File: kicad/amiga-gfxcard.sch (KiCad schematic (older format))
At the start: 33 parts, among them P1 CONN_01X04, P2 CONN_01X16, P3 CONN_01X16, P4 CONN_01X16, P5 CONN_01X04, P6 CONN_01X04, P7 CONN_01X08, U1 TXB0108, U10 SN74CBT16233, U12 VGA, U2 TXB0108, U3 TXB0108, U4 TXB0108, U5 TXB0108, U6 TXB0108, U7 ADV7125-lqfp48, U8 SN74CBT16233, U9 74LS04

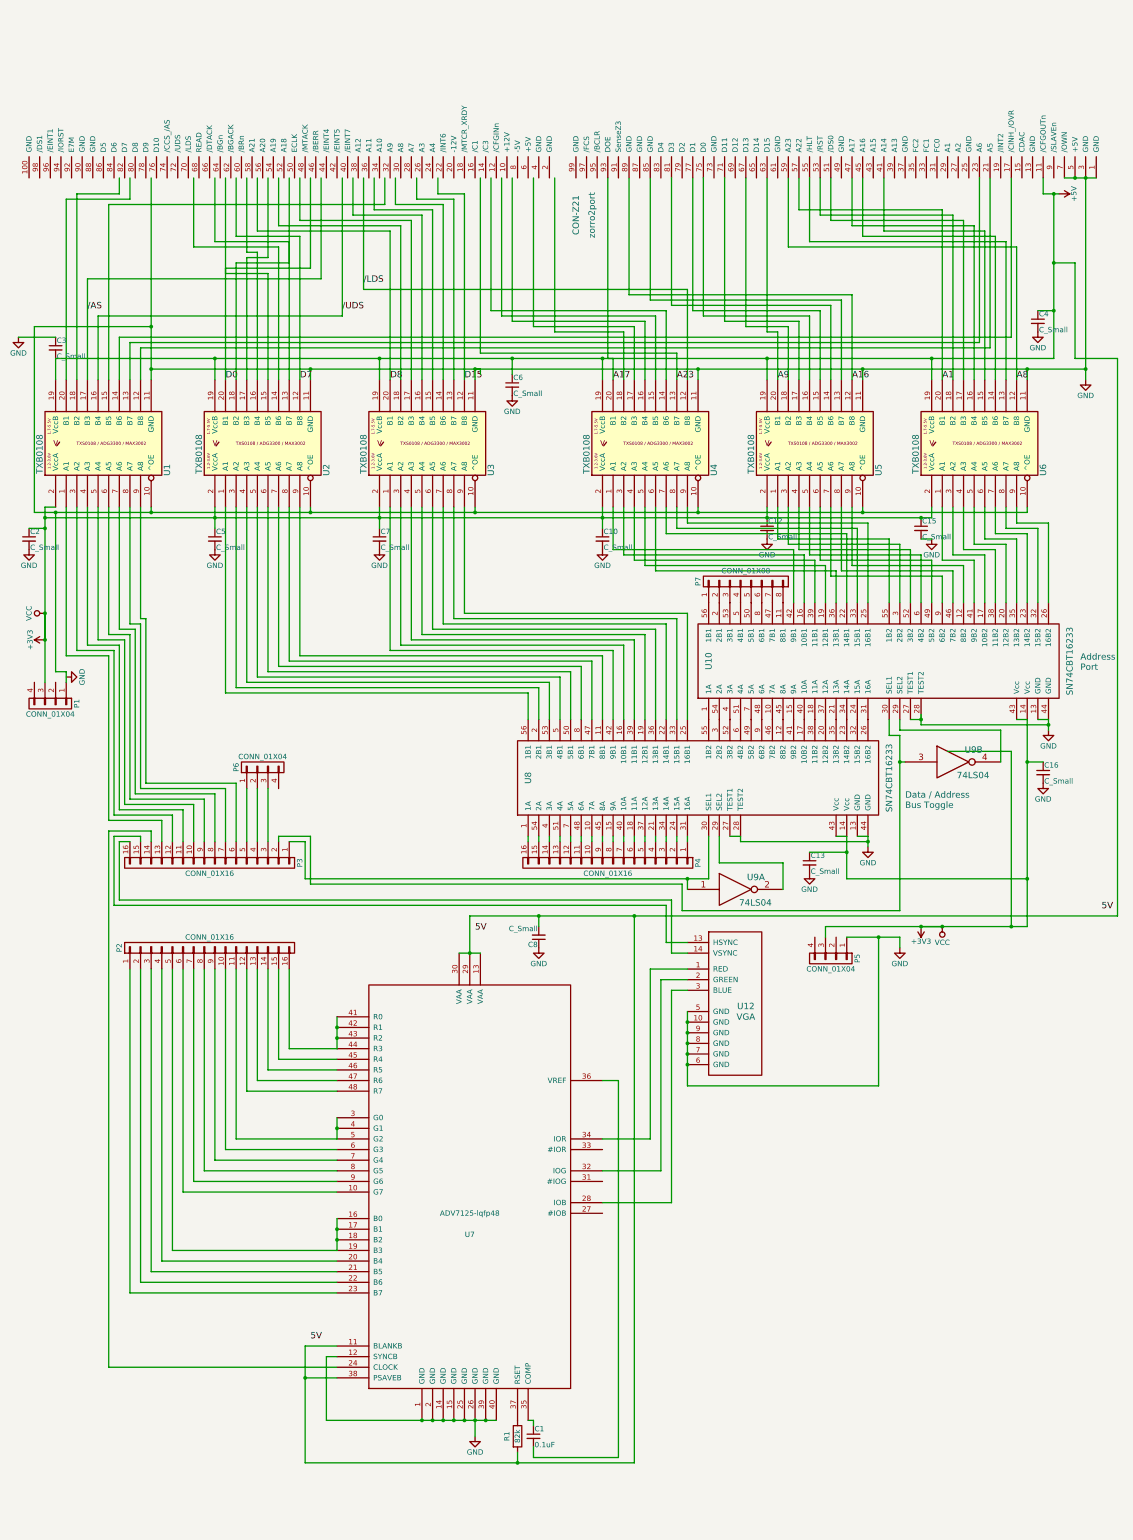
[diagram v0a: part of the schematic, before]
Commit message: WIP of simpler redesign for miniSpartan 6+
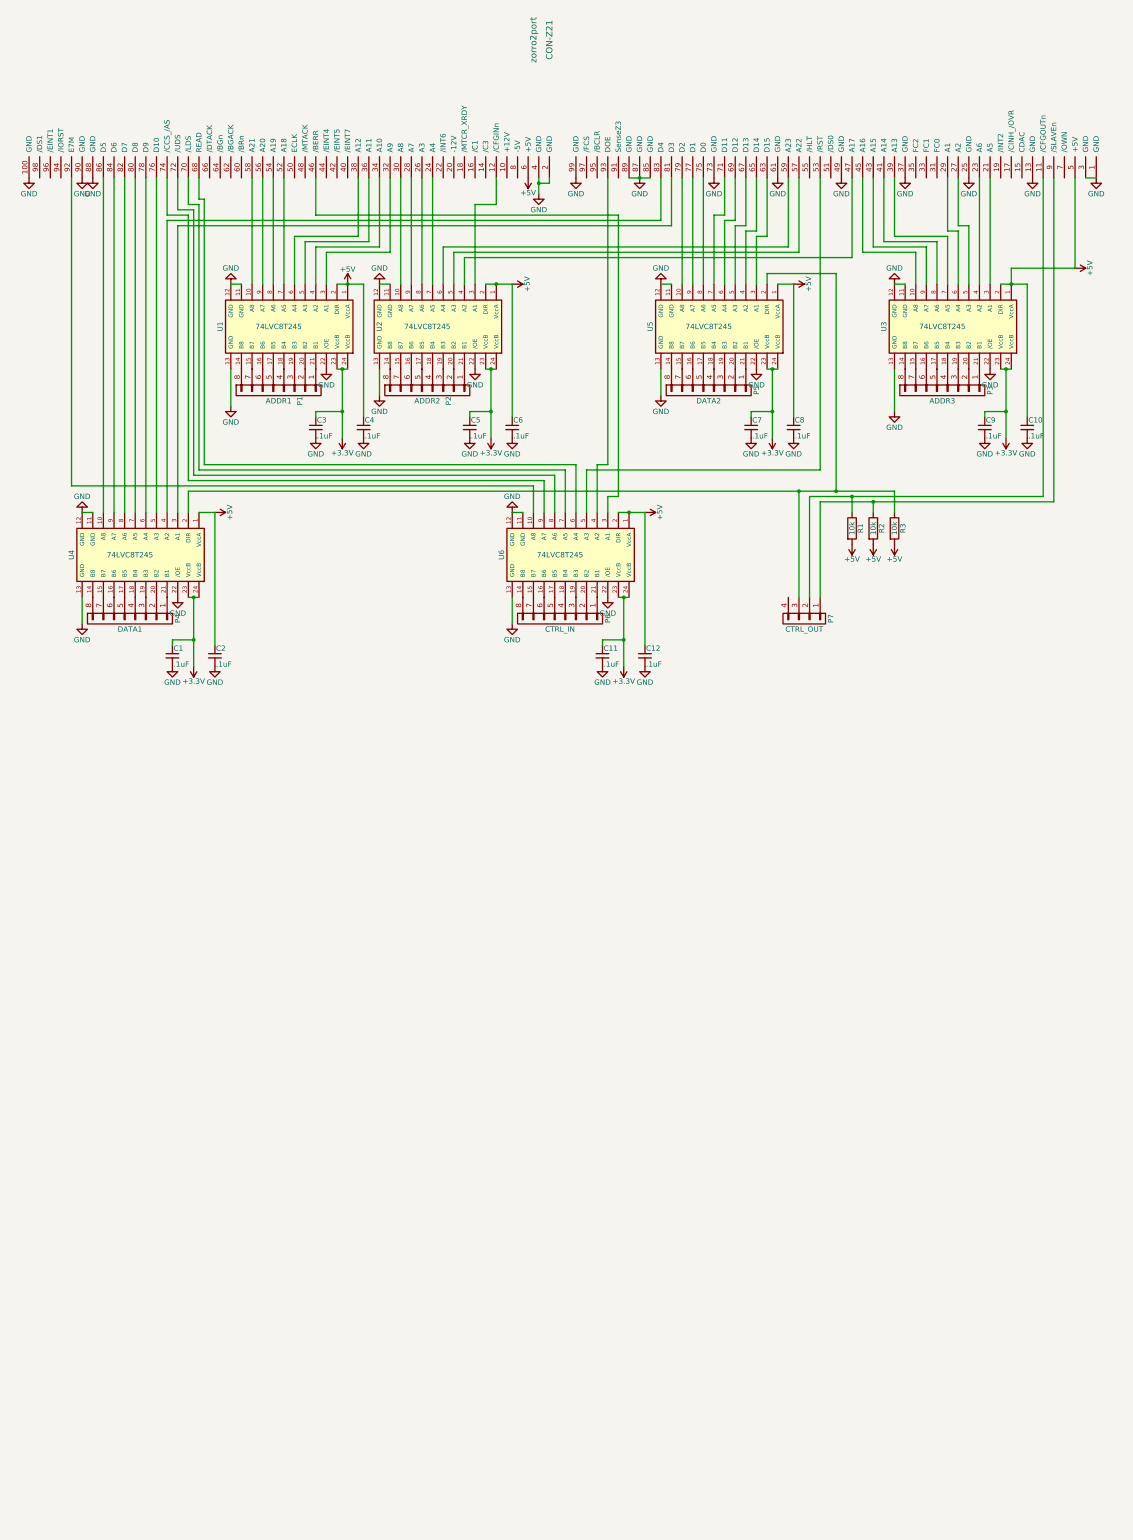
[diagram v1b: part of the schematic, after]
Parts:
- removed C13, C15, C16: C_Small, Capacitors_SMD:C_0603_HandSoldering, symbol C_Small
- removed P1, P5, P6: CONN_01X04, Pin_Headers:Pin_Header_Straight_1x04, symbol CONN_01X04
- removed P2, P3, P4: CONN_01X16, Pin_Headers:Pin_Header_Straight_1x16, symbol CONN_01X16
- removed U1, U2, U3, U4, U5, U6: TXB0108, opendous:TSSOP20_PW, symbol TXB0108
- removed U10, U8: SN74CBT16233, Housings_SSOP:SSOP-56_7.5x18.5mm_Pitch0.635mm, symbol SN74CBT16233
- removed U12: VGA, zorro2:HD15_B-HD15F, symbol VGA
- removed U7: ADV7125-lqfp48, Housings_QFP:LQFP-48_7x7mm_Pitch0.5mm, symbol ADV7125-lqfp48
- removed U9: 74LS04, Housings_SSOP:SSOP-14_5.3x6.2mm_Pitch0.65mm, symbol 74LS04
- added C11, C9: .1uF, Capacitors_ThroughHole:C_Rect_L4_W2.5_P2.5, symbol C_Small
- added P1: ADDR1, Pin_Headers:Pin_Header_Straight_1x08, symbol CONN_01X08
- added P2: ADDR2, Pin_Headers:Pin_Header_Straight_1x08, symbol CONN_01X08
- added P3: ADDR3, Pin_Headers:Pin_Header_Straight_1x08, symbol CONN_01X08
- added P5: DATA2, Pin_Headers:Pin_Header_Straight_1x08, symbol CONN_01X08
- added P6: CTRL_IN, Pin_Headers:Pin_Header_Straight_1x08, symbol CONN_01X08
- added P7: CTRL_OUT, Pin_Headers:Pin_Header_Straight_1x04, symbol CONN_01X04
- added R2, R3: 10k, Resistors_ThroughHole:Resistor_Horizontal_RM7mm, symbol R
- added U1, U2, U3, U4, U5, U6: 74LVC8T245, mnt:TSSOP24-44, symbol 74LVC8T245
- C1: value 0.1uF -> .1uF; footprint Capacitors_ThroughHole:C_Disc_D3_P2.5 -> Capacitors_ThroughHole:C_Rect_L4_W2.5_P2.5
- C10, C12, C2, C3, C4, C5, C6, C7, C8: value C_Small -> .1uF; footprint Capacitors_SMD:C_0603_HandSoldering -> Capacitors_ThroughHole:C_Rect_L4_W2.5_P2.5
- P4: renamed from P7; value CONN_01X08 -> DATA1
- R1: value 82k -> 10k; footprint Resistors_ThroughHole:Resistor_Horizontal_RM10mm -> Resistors_ThroughHole:Resistor_Horizontal_RM7mm
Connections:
- net labels added: +3.3V
- net labels removed: +3V3, /AS, /LDS, /UDS, 5V, A1, A16, A17, A23, A8, A9, D0, D15, D7, D8, VCC
- wire segments 517 -> 187
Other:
- note removed: "Address\nPort"
- note removed: "Data / Address \nBus Toggle"
- moved on the sheet: C4, P4

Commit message: redo of mk2 board finished
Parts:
- added P10: AUX1B, Pin_Headers:Pin_Header_Straight_1x08, symbol CONN_01X08
- added P11: AUX2A, Pin_Headers:Pin_Header_Straight_1x04, symbol CONN_01X04
- added P12: AUX2B, Pin_Headers:Pin_Header_Straight_1x04, symbol CONN_01X04
- added P8: CONN_01X02, Pin_Headers:Pin_Header_Straight_1x02, symbol CONN_01X02
- added P9: AUX1A, Pin_Headers:Pin_Header_Straight_1x08, symbol CONN_01X08
- C1, C10, C11, C12, C2, C3, C4, C5, C6, C7, C8, C9: footprint Capacitors_ThroughHole:C_Rect_L4_W2.5_P2.5 -> Capacitors_SMD:C_0805_HandSoldering
- P3: value ADDR3 -> ADDR4
- P4: value DATA1 -> DATA2
- P5: value DATA2 -> ADDR3
- P6: value CTRL_IN -> DATA1
- R1, R2, R3: footprint Resistors_ThroughHole:Resistor_Horizontal_RM7mm -> Resistors_SMD:R_1206_HandSoldering
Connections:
- net +3V3: now also P8.2 (P2)
- net +5V: now also U5.2 (DIR); no longer U2.2 (DIR)
- net GND: now also P8.1 (P1)
- net at CON-Z21.11 (/CFGOUTn), R1.1: now also P7.1 (P1); no longer P7.2 (P2)
- net at CON-Z21.21 (A5): now also U1.10 (A8); no longer U3.3 (A1)
- net at CON-Z21.23 (A6): now also U1.9 (A7); no longer U3.4 (A2)
- net at CON-Z21.24 (A4): now also U5.10 (A8); no longer U2.7 (A5)
- net at CON-Z21.26 (A3): now also U5.9 (A7); no longer U2.8 (A6)
- net at CON-Z21.27 (A2): now also U1.8 (A6); no longer U3.5 (A3)
- net at CON-Z21.28 (A7): now also U5.8 (A6); no longer U2.9 (A7)
- net at CON-Z21.29 (A1): now also U1.7 (A5); no longer U3.6 (A4)
- net at CON-Z21.30 (A8): now also U5.7 (A5); no longer U2.10 (A8)
- net at CON-Z21.32 (A9): now also U5.6 (A4); no longer U1.3 (A1)
- net at CON-Z21.34 (A10): now also U5.5 (A3); no longer U1.4 (A2)
- net at CON-Z21.36 (A11): now also U5.4 (A2); no longer U1.5 (A3)
- net at CON-Z21.38 (A12): now also U5.3 (A1); no longer U1.6 (A4)
- net at CON-Z21.39 (A13): now also U1.6 (A4); no longer U3.7 (A5)
- net at CON-Z21.41 (A14): now also U1.5 (A3); no longer U3.8 (A6)
- net at CON-Z21.43 (A15): now also U1.4 (A2); no longer U3.9 (A7)
- net at CON-Z21.45 (A16): now also U1.3 (A1); no longer U3.10 (A8)
- net at CON-Z21.46 (/BERR): now also U2.4 (A2); no longer U6.3 (A1)
- net at CON-Z21.47 (A17): now also U2.10 (A8); no longer U2.4 (A2)
- net at CON-Z21.52 (A18): now also U3.10 (A8); no longer U1.7 (A5)
- net at CON-Z21.53 (/RST): now also U2.5 (A3); no longer U6.5 (A3)
- net at CON-Z21.54 (A19): now also U3.9 (A7); no longer U1.8 (A6)
- net at CON-Z21.56 (A20): now also U3.8 (A6); no longer U1.9 (A7)
- net at CON-Z21.57 (A22): now also U2.9 (A7); no longer U2.5 (A3)
- net at CON-Z21.58 (A21): now also U3.7 (A5); no longer U1.10 (A8)
- net at CON-Z21.59 (A23): now also U2.8 (A6); no longer U2.6 (A4)
- net at CON-Z21.63 (D15): now also U6.10 (A8); no longer U5.3 (A1)
- net at CON-Z21.65 (D14): now also U6.9 (A7); no longer U5.4 (A2)
- net at CON-Z21.67 (D13): now also U6.8 (A6); no longer U5.5 (A3)
- net at CON-Z21.68 (READ): now also U3.6 (A4); no longer U6.6 (A4)
- net at CON-Z21.69 (D12): now also U6.7 (A5); no longer U5.6 (A4)
- net at CON-Z21.70 (/LDS): now also U3.5 (A3); no longer U6.7 (A5)
- net at CON-Z21.71 (D11): now also U6.6 (A4); no longer U5.7 (A5)
- net at CON-Z21.72 (/UDS): now also U3.4 (A2); no longer U6.8 (A6)
- net at CON-Z21.74 (/CCS_/AS): now also U3.3 (A1); no longer U6.9 (A7)
- net at CON-Z21.75 (D0): now also U6.5 (A3); no longer U5.8 (A6)
- net at CON-Z21.76 (D10): now also U4.10 (A8); no longer U4.5 (A3)
- net at CON-Z21.77 (D1): now also U6.4 (A2); no longer U5.9 (A7)
- net at CON-Z21.78 (D9): now also U4.9 (A7); no longer U4.6 (A4)
- net at CON-Z21.79 (D2): now also U6.3 (A1); no longer U5.10 (A8)
- net at CON-Z21.80 (D8): now also U4.8 (A6); no longer U4.7 (A5)
- net at CON-Z21.81 (D3): now also U4.4 (A2); no longer U4.3 (A1)
- net at CON-Z21.82 (D7): now also U4.7 (A5); no longer U4.8 (A6)
- net at CON-Z21.83 (D4): now also CON-Z21.92 (E7M), U2.6 (A4), U4.3 (A1); no longer U4.4 (A2)
- net at CON-Z21.84 (D6): now also U4.6 (A4); no longer U4.9 (A7)
- net at CON-Z21.86 (D5): now also U4.5 (A3); no longer U4.10 (A8)
- net at CON-Z21.9 (/SLAVEn), R2.1: now also P7.2 (P2); no longer P7.1 (P1)
- net at CON-Z21.93 (DOE): now also U2.7 (A5); no longer U6.4 (A2)
- net at R3.1, U4.2 (DIR): now also P7.4 (P4), U2.2 (DIR); no longer P7.3 (P3), U5.2 (DIR)
- new net: P10.1 (P1), P9.1 (P1)
- new net: P10.2 (P2), P9.2 (P2)
- new net: P10.3 (P3), P9.3 (P3)
- new net: P10.4 (P4), P9.4 (P4)
- new net: P10.5 (P5), P9.5 (P5)
- new net: P10.6 (P6), P9.6 (P6)
- new net: P10.7 (P7), P9.7 (P7)
- new net: P10.8 (P8), P9.8 (P8)
- new net: P11.1 (P1), P12.1 (P1)
- new net: P11.2 (P2), P12.2 (P2)
- new net: P11.3 (P3), P12.3 (P3)
- new net: P11.4 (P4), P12.4 (P4)
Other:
- moved on the sheet: C1, C10, C11, C12, C2, C3, C4, C5, C6, C7, C8, C9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

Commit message: board v1.2 finished
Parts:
- removed P10: AUX1B, Pin_Headers:Pin_Header_Straight_1x08, symbol CONN_01X08
- removed P11: AUX2A, Pin_Headers:Pin_Header_Straight_1x04, symbol CONN_01X04
- removed P12: AUX2B, Pin_Headers:Pin_Header_Straight_1x04, symbol CONN_01X04
- removed P7: CTRL_OUT, Pin_Headers:Pin_Header_Straight_1x04, symbol CONN_01X04
- removed P9: AUX1A, Pin_Headers:Pin_Header_Straight_1x08, symbol CONN_01X08
- added P13: X1, Pin_Headers:Pin_Header_Straight_1x08, symbol CONN_01X08
- added P14: X2, Pin_Headers:Pin_Header_Straight_1x08, symbol CONN_01X08
- added P16: D1, Pin_Headers:Pin_Header_Straight_1x03, symbol CONN_01X03
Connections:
- net +5V: now also U2.2 (DIR); no longer U6.2 (DIR)
- net at CON-Z21.11 (/CFGOUTn), R1.1: now also P16.1 (P1)
- net at CON-Z21.83 (D4), U4.3 (A1): no longer CON-Z21.92 (E7M), U2.6 (A4)
- net at CON-Z21.9 (/SLAVEn), R2.1: now also P16.2 (P2)
- net at P4.1 (P1): no longer U4.21 (B1)
- net at P4.5 (P5): no longer U4.17 (B5)
- net at P1.1 (P1): no longer U1.21 (B1)
- net at P1.5 (P5): no longer U1.17 (B5)
- net at P2.1 (P1): no longer U2.21 (B1)
- net at P2.5 (P5): no longer U2.17 (B5)
- net at P6.1 (P1): no longer U6.21 (B1)
- net at P6.5 (P5): no longer U6.17 (B5)
- net at P5.1 (P1): no longer U5.21 (B1)
- net at P5.5 (P5): no longer U5.17 (B5)
- net at P3.1 (P1): no longer U3.21 (B1)
- net at P3.5 (P5): no longer U3.17 (B5)
- net at R3.1, U4.2 (DIR): now also U6.2 (DIR), P16.3 (P3); no longer U2.2 (DIR)
- new net: CON-Z21.92 (E7M), U2.6 (A4)
- new net: P13.8 (P8), U1.17 (B5)
- new net: P13.7 (P7), U1.21 (B1)
- new net: P14.8 (P8), U2.17 (B5)
- new net: P14.7 (P7), U2.21 (B1)
- new net: P14.6 (P6), U5.17 (B5)
- new net: P14.4 (P4), U5.21 (B1)
- new net: P14.3 (P3), U3.17 (B5)
- new net: P14.2 (P2), U3.21 (B1)
- new net: P13.6 (P6), U4.17 (B5)
- new net: P13.4 (P4), U4.21 (B1)
- new net: P13.3 (P3), U6.17 (B5)
- new net: P13.2 (P2), U6.21 (B1)
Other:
- moved on the sheet: C11, C12, C3, C4, C5, C6, P1, P2, P3, P4, P5, P6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

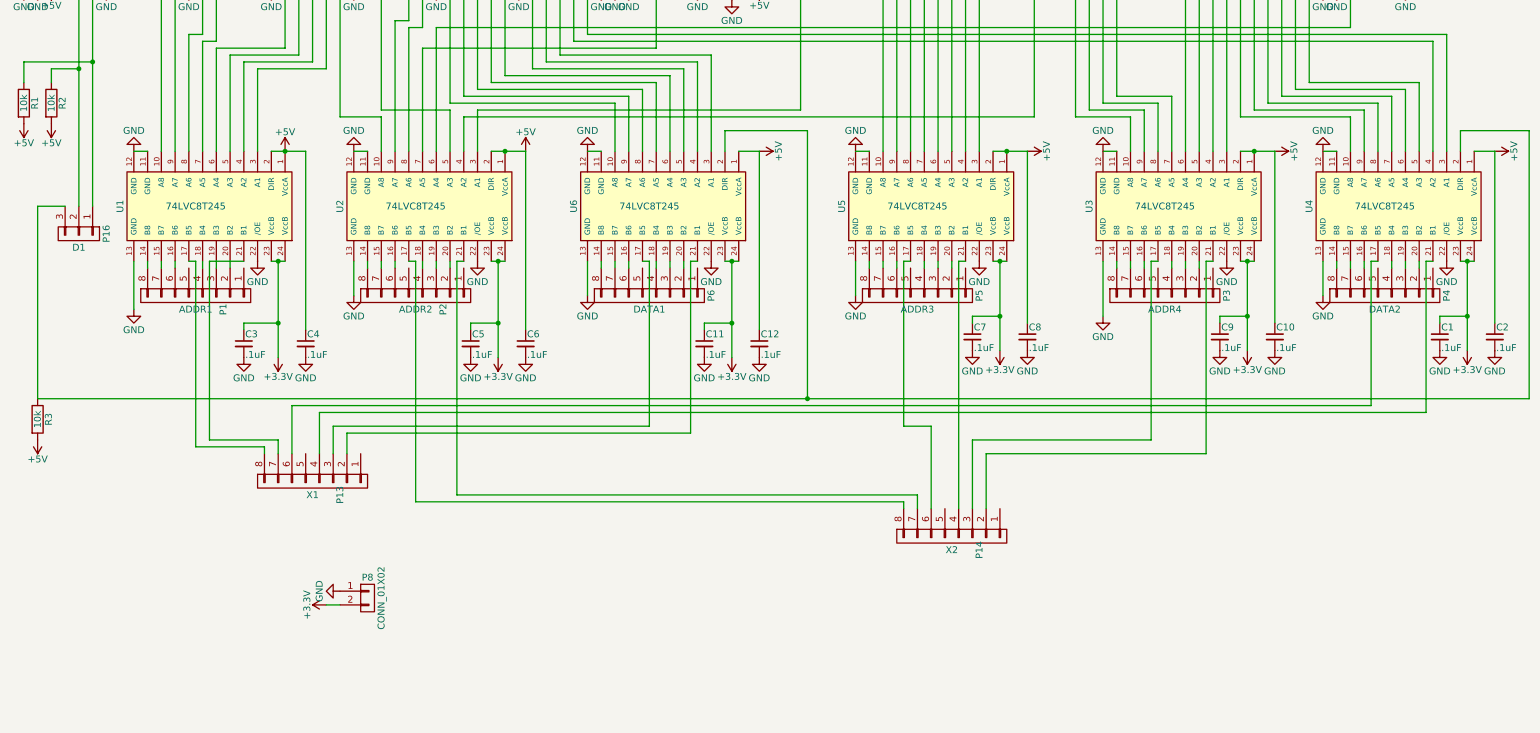
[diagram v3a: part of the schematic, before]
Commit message: Version 2, new board, minispartan 6+, working DVI/HDMI output
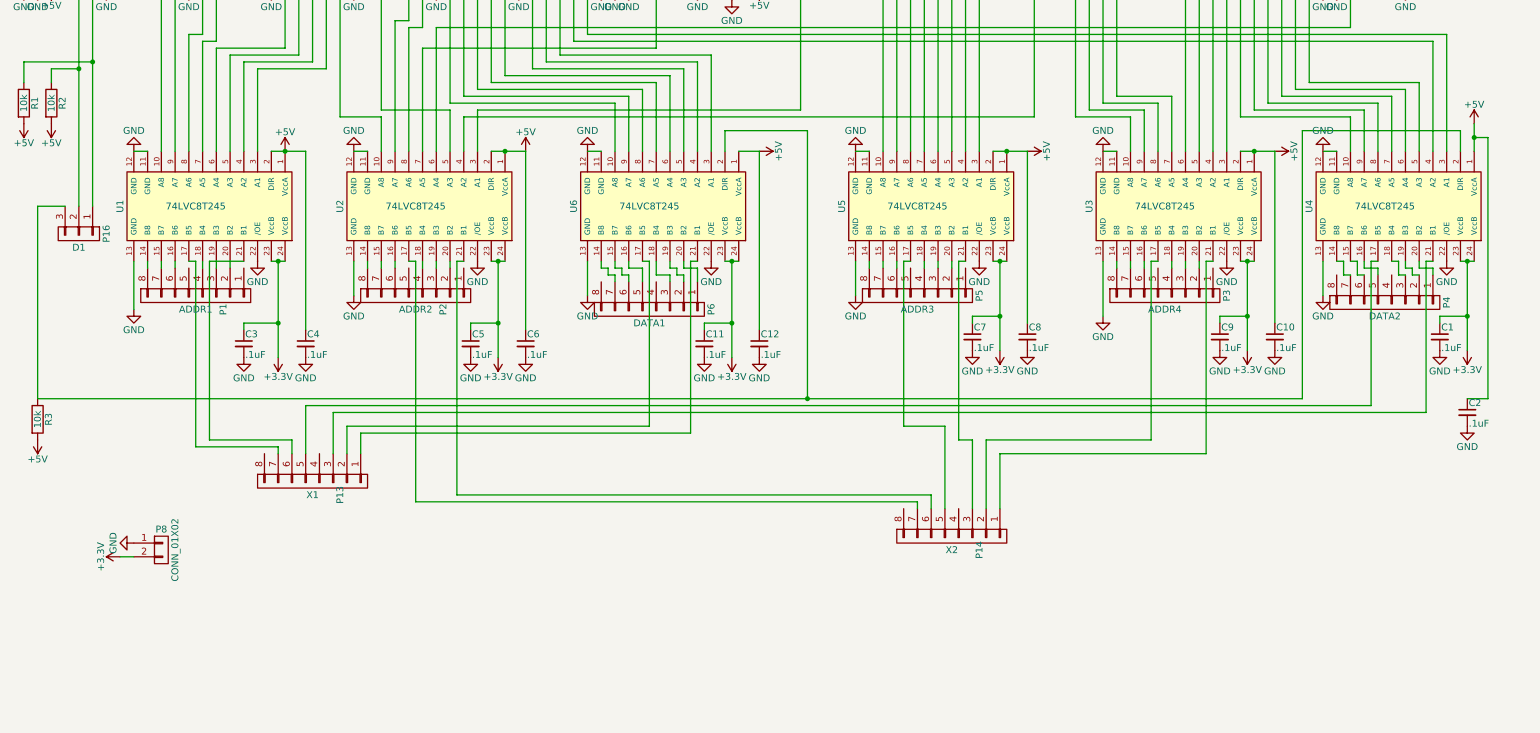
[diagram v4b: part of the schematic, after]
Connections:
- net at P4.1 (P1): now also U4.20 (B2)
- net at P4.2 (P2): now also U4.19 (B3); no longer U4.20 (B2)
- net at P4.3 (P3): now also U4.18 (B4); no longer U4.19 (B3)
- net at P4.4 (P4): no longer U4.18 (B4)
- net at P4.5 (P5): now also U4.16 (B6)
- net at P4.6 (P6): now also U4.15 (B7); no longer U4.16 (B6)
- net at P4.7 (P7): now also U4.14 (B8); no longer U4.15 (B7)
- net at P4.8 (P8): no longer U4.14 (B8)
- net at P6.1 (P1): now also U6.20 (B2)
- net at P6.2 (P2): now also U6.19 (B3); no longer U6.20 (B2)
- net at P6.3 (P3): now also U6.18 (B4); no longer U6.19 (B3)
- net at P6.4 (P4): no longer U6.18 (B4)
- net at P6.5 (P5): now also U6.16 (B6)
- net at P6.6 (P6): now also U6.15 (B7); no longer U6.16 (B6)
- net at P6.7 (P7): now also U6.14 (B8); no longer U6.15 (B7)
- net at P6.8 (P8): no longer U6.14 (B8)
- net at U1.17 (B5): now also P13.7 (P7); no longer P13.8 (P8)
- net at U1.21 (B1): now also P13.6 (P6); no longer P13.7 (P7)
- net at U2.17 (B5): now also P14.7 (P7); no longer P14.8 (P8)
- net at U2.21 (B1): now also P14.6 (P6); no longer P14.7 (P7)
- net at U5.17 (B5): now also P14.5 (P5); no longer P14.6 (P6)
- net at U5.21 (B1): now also P14.3 (P3); no longer P14.4 (P4)
- net at U3.17 (B5): now also P14.2 (P2); no longer P14.3 (P3)
- net at U3.21 (B1): now also P14.1 (P1); no longer P14.2 (P2)
- net at U4.17 (B5): now also P13.5 (P5); no longer P13.6 (P6)
- net at U4.21 (B1): now also P13.3 (P3); no longer P13.4 (P4)
- net at U6.17 (B5): now also P13.2 (P2); no longer P13.3 (P3)
- net at U6.21 (B1): now also P13.1 (P1); no longer P13.2 (P2)
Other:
- moved on the sheet: C2, P4, P6, P8
